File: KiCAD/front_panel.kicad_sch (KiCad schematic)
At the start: 2 parts, among them U15 Adafruit_PCF8575_Breakout

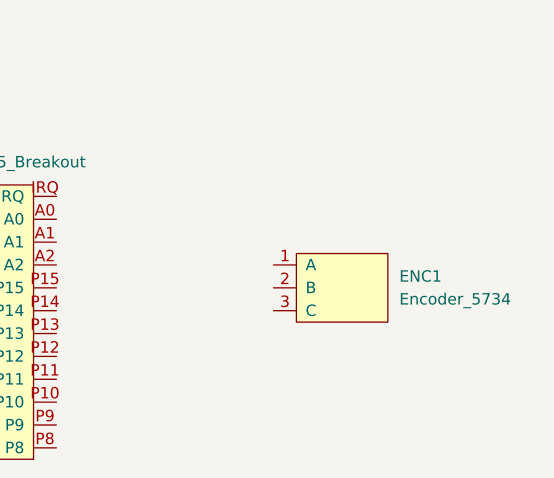
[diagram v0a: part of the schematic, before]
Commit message: schematic: I2C topology flip + CD14538B heartbeat + pre-layout audit
- Documentation updates for the STEMMA-QT topology flip (MCP4728 upstream
  of Si5351): design_review_7-5-26 C1 marked resolved, build_checklist
  Phase 1 gets the 6-step first-boot procedure, cw_envelope_keyer I2C
  address section rewritten, front_panel_interface signal-chain diagram
  refreshed.
- CD14538B dual retriggerable monostable added to xmitter.kicad_sym
  (PDIP-16, pinout verified against datasheet fig. 1), plus datasheet
  file.
- Arduino sheet: CD14538B heartbeat topology on Q5 HV contactor -- U18
  + R30 470K + C41 1uF timing (t_w ~470 ms), Q7 series FET stack,
  C42/C43 VDD bypass and bulk.
- Pre-layout audit output as Documentation/punch_list_7-6-26.txt (list
  of blockers before PCB layout, ordered by severity).

Co-Authored-By: Claude Opus 4.7 (1M context) <noreply@anthropic.com>
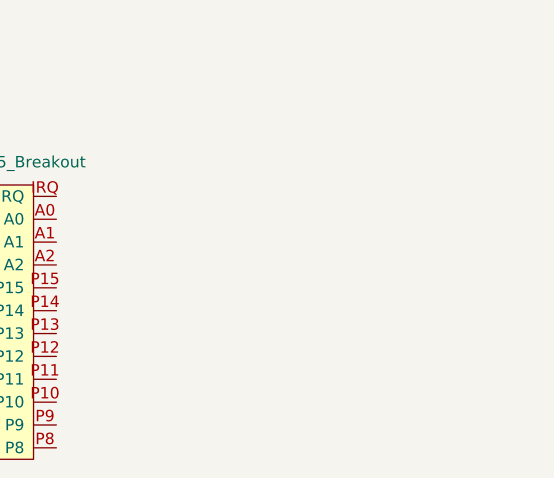
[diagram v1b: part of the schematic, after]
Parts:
- removed ENC1: Encoder_5734, Connector_PinHeader_2.54mm:PinHeader_1x03_P2.54mm_Vertical, symbol xmitter:Encoder_5734
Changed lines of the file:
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@@
-		)
-	)
-	(symbol
-		(lib_id "xmitter:Encoder_5734")
-		(at 182.88 87.63 0)
-		(unit 1)
-		(body_style 1)
-		(exclude_from_sim no)
-		(in_bom yes)
-		(on_board yes)
-		(in_pos_files yes)
-		(dnp no)
-		(fields_autoplaced yes)
-		(property "Reference" "ENC1"
-			(at 189.23 86.3599 0)
-			(show_name no)
-			(do_not_autoplace no)
-			(effects
-				(font
-					(size 1.27 1.27)
-				)
-				(justify left)
-			)
-		)
-		(property "Value" "Encoder_5734"
-			(at 189.23 88.8999 0)
-			(show_name no)
-			(do_not_autoplace no)
-			(effects
-				(font
-					(size 1.27 1.27)
-				)
-				(justify left)
-			)
-		)
-		(property "Footprint" "Connector_PinHeader_2.54mm:PinHeader_1x03_P2.54mm_Vertical"
-			(at 182.88 87.63 0)
-			(hide yes)
-			(show_name no)
-			(do_not_autoplace no)
-			(effects
-				(font
-					(size 1.27 1.27)
-				)
-			)
-		)
-		(property "Datasheet" "https://www.adafruit.com/product/5734"
-			(at 182.88 87.63 0)
-			(hide yes)
-			(show_name no)
-			(do_not_autoplace no)
-			(effects
-				(font
-					(size 1.27 1.27)
-				)
-			)
-		)
-		(property "Description" "60mm rugged rotary encoder, 100 PPR, screw terminals, no switch"
-			(at 182.88 87.63 0)
-			(hide yes)
-			(show_name no)
-			(do_not_autoplace no)
-			(effects
-				(font
-					(size 1.27 1.27)
-				)
-			)
-		)
-		(property "Manufacturer" "Adafruit Industries"
-			(at 182.88 87.63 0)
-			(hide yes)
-			(show_name no)
-			(do_not_autoplace no)
-			(effects
-				(font
-					(size 1.27 1.27)
-				)
-			)
-		)
-		(property "MPN" "Adafruit #5734"
-			(at 182.88 87.63 0)
-			(hide yes)
-			(show_name no)
-			(do_not_autoplace no)
-			(effects
-				(font
-					(size 1.27 1.27)
-				)
-			)
-		)
-		(pin "1"
-		)
-		(pin "2"
-		)
-		(pin "3"
-		)
-		(instances
-			(project "KiCAD"
-				(path "/d3de40b8-856b-4fbd-829c-f45ffcd55742/6a4b1c9d-2e3f-4b5a-8c7d-1e2f3a4b5c6d"
-					(reference "ENC1")
-					(unit 1)
-				)
-			)
 		)
 	)

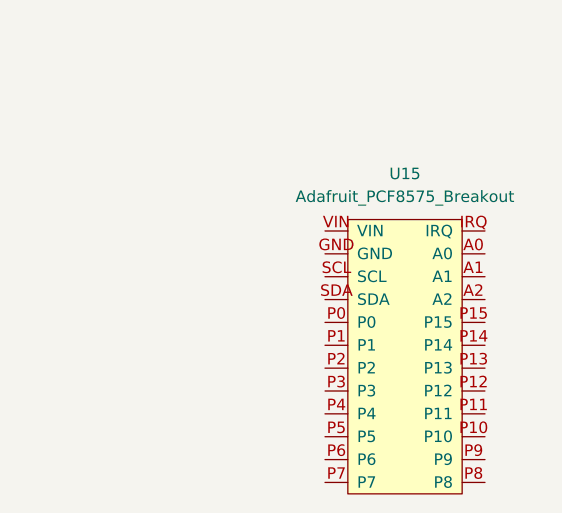
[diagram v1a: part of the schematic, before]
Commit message: kicad: PWR_FLAGs added, most +3.3V converted to 3V3, VFO renames + J2 NC
User work today:
- Placed PWR_FLAGs to silence "power_pin_not_driven" ERC errors for VEE,
  +12V, -90V rails (see B5a-B5f in the punch list)
- Converted 6 of 7 +3.3V power symbols to 3V3 global labels project-wide
  (one +3.3V remains on bias sheet, resolves next pass)
- VFO sheet: C_coup -> C_IN1, R6 -> RD1 (both were unannotated / duplicate
  ref designators; ERC B4a and B4b now resolved)
- buffer_keyer: J2 pin 2 gets a no_connect flag (B4c resolved); TP2 and
  TP7 electrically wired to MOD_RF_OUT+/- via junctions (B4d/e resolved)

Punch list updates:
- B3 (footprints) marked done
- B4a/b/c marked done
- M5 (TX LED) confirmed resolved (external LED across T/R relay coil)
- B2 (paddle) rewritten for the actual 2-conductor 1/4" plug scheme

Current ERC status: 61 errors, 0 warnings (from 74 + 2 originally).
Remaining real bugs: unannotated C_IN + duplicate C_IN1 on buffer_keyer,
misplaced #FLG04 on Metro's 3V3 pin, one leftover +3.3V on bias. Rest
are the known-non-issue plateau.

Co-Authored-By: Claude Opus 4.7 (1M context) <noreply@anthropic.com>
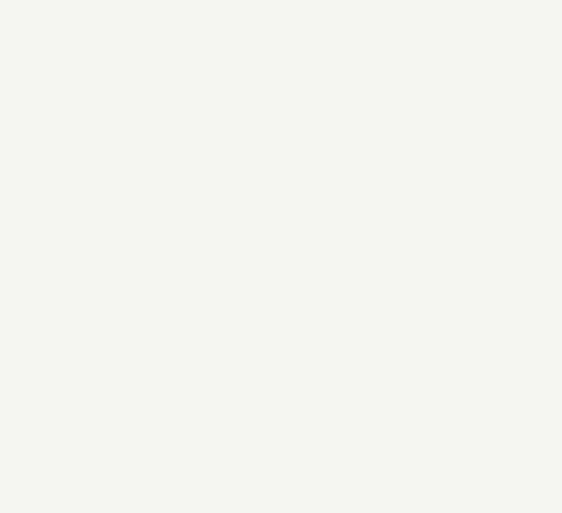
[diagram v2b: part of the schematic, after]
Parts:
- removed U15: Adafruit_PCF8575_Breakout, xmitter:Adafruit_PCF8575_Breakout, symbol xmitter:Adafruit_PCF8575_Breakout
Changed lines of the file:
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@@
-		)
-	)
-	(symbol
-		(lib_id "xmitter:Adafruit_PCF8575_Breakout")
-		(at 142.24 91.44 0)
-		(unit 1)
-		(body_style 1)
-		(exclude_from_sim no)
-		(in_bom yes)
-		(on_board yes)
-		(in_pos_files yes)
-		(dnp no)
-		(fields_autoplaced yes)
-		(property "Reference" "U15"
-			(at 142.24 71.12 0)
-			(show_name no)
-			(do_not_autoplace no)
-			(effects
-				(font
-					(size 1.27 1.27)
-				)
-			)
-		)
-		(property "Value" "Adafruit_PCF8575_Breakout"
-			(at 142.24 73.66 0)
-			(show_name no)
-			(do_not_autoplace no)
-			(effects
-				(font
-					(size 1.27 1.27)
-				)
-			)
-		)
-		(property "Footprint" "xmitter:Adafruit_PCF8575_Breakout"
-			(at 142.24 91.44 0)
-			(hide yes)
-			(show_name no)
-			(do_not_autoplace no)
-			(effects
-				(font
-					(size 1.27 1.27)
-				)
-			)
-		)
-		(property "Datasheet" "https://learn.adafruit.com/adafruit-pcf8575"
-			(at 142.24 91.44 0)
-			(hide yes)
-			(show_name no)
-			(do_not_autoplace no)
-			(effects
-				(font
-					(size 1.27 1.27)
-				)
-			)
-		)
-		(property "Description" "Adafruit PCF8575 I2C 16-GPIO expander breakout (PID 5904), default I2C addr 0x20"
-			(at 142.24 91.44 0)
-			(hide yes)
-			(show_name no)
-			(do_not_autoplace no)
-			(effects
-				(font
-					(size 1.27 1.27)
-				)
-			)
-		)
-		(property "Manufacturer" "Adafruit Industries"
-			(at 142.24 91.44 0)
-			(hide yes)
-			(show_name no)
-			(do_not_autoplace no)
-			(effects
-				(font
-					(size 1.27 1.27)
-				)
-			)
-		)
-		(property "MPN" "Adafruit #5904"
-			(at 142.24 91.44 0)
-			(hide yes)
-			(show_name no)
-			(do_not_autoplace no)
-			(effects
-				(font
-					(size 1.27 1.27)
-				)
-			)
-		)
-		(pin "A0"
-		)
-		(pin "P10"
-		)
-		(pin "P4"
-		)
-		(pin "P5"
-		)
-		(pin "VIN"
-		)
-		(pin "P7"
-		)
-		(pin "A1"
-		)
-		(pin "A2"
-		)
-		(pin "IRQ"
-		)
-		(pin "P2"
-		)
-		(pin "P1"
-		)
-		(pin "P8"
-		)
-		(pin "P9"
-		)
-		(pin "GND"
-		)
-		(pin "P3"
-		)
-		(pin "P12"
-		)
-		(pin "P13"
-		)
-		(pin "P6"
-		)
-		(pin "P11"
-		)
-		(pin "P14"
-		)
-		(pin "P0"
-		)
-		(pin "SDA"
-		)
-		(pin "P15"
-		)
-		(pin "SCL"
-		)
-		(instances
-			(project "KiCAD"
-				(path "/d3de40b8-856b-4fbd-829c-f45ffcd55742/6a4b1c9d-2e3f-4b5a-8c7d-1e2f3a4b5c6d"
-					(reference "U15")
-					(unit 1)
-				)
-			)
 		)
 	)
